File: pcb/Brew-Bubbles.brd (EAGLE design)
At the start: 25.5 x 28.7 mm, 10 parts, among them U1 GP1A57HR, U2 WEMOS-D1-MINI

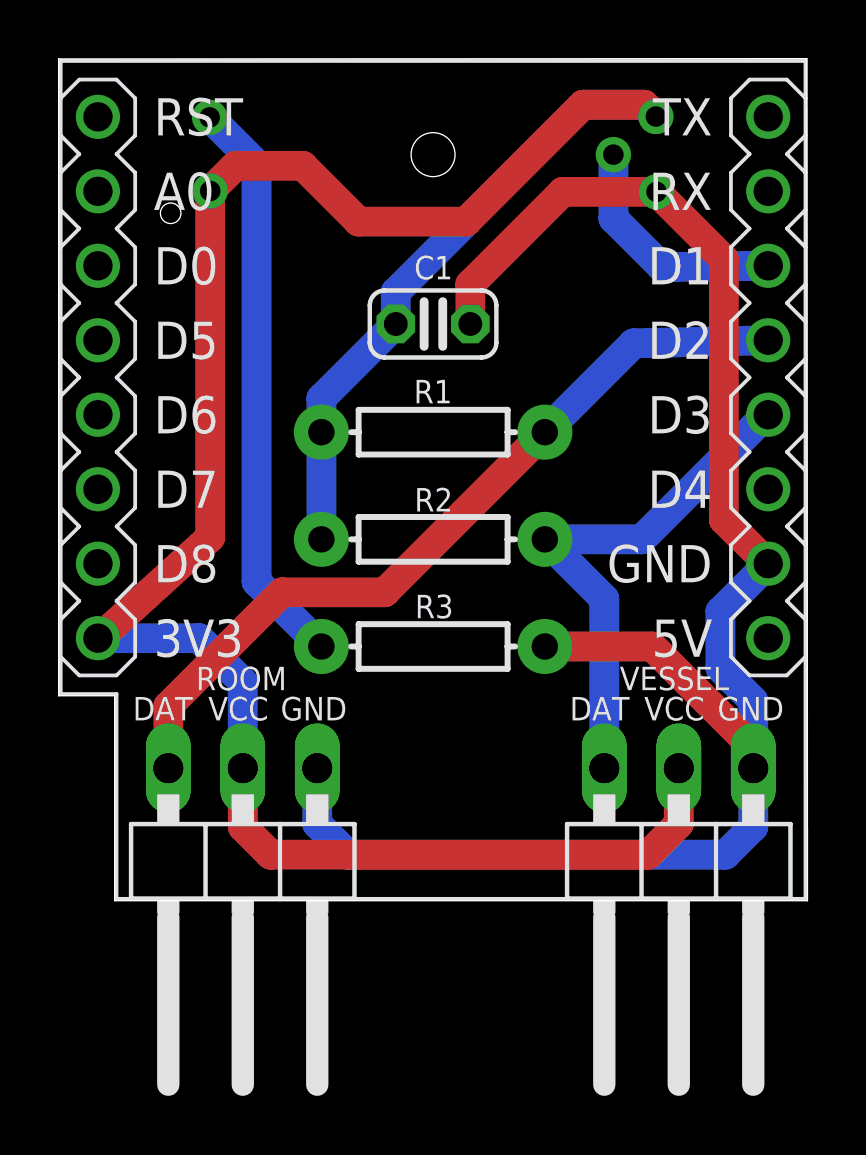
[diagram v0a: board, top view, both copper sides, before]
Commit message: Add decoupling caps to 3v3 and 5v
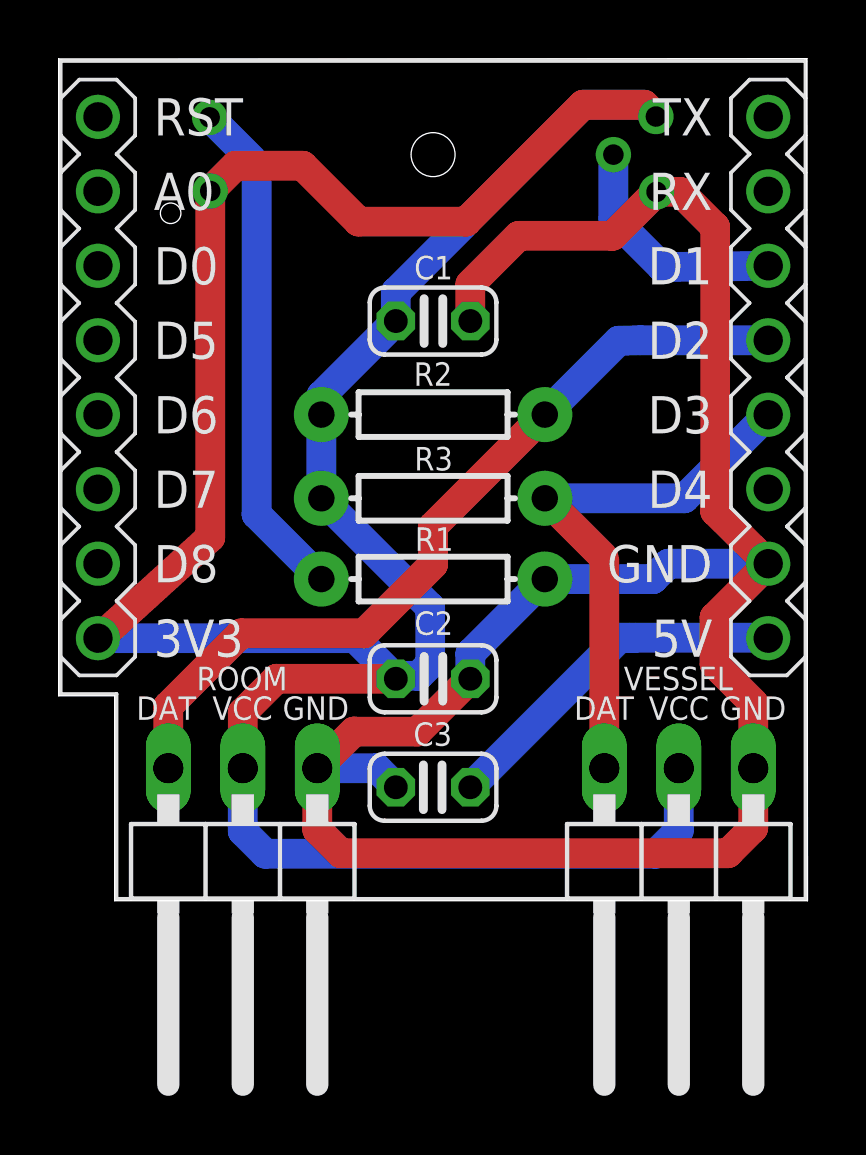
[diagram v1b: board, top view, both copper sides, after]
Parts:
- added C2, C3: 0.1μF, rcl:C025-024X044
- R1: value 2.2kΩ -> 150Ω
- R3: value 150Ω -> 2.2kΩ
- moved R3 5.05 mm to (12.8, 13.8)
- moved R1 5.01 mm to (12.8, 11.0)
- moved R2 4.25 mm to (12.8, 16.6)
- moved C1 0.10 mm to (12.8, 19.8)
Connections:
- net 3V3: now also C2.1, R3.P$2; no longer R1.P$2
- net 5V: now also C3.1
- net D2: now also R2.P$1; no longer R1.P$1
- net D3: now also R3.P$1; no longer R2.P$1
- net GND: now also C2.2, C3.2, R1.P$1; no longer R3.P$1
- net PD1: now also R1.P$2; no longer R3.P$2
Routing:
- net 3V3: track 84.5 -> 101.7 mm
- net GND: track 60.2 -> 73.3 mm
- net 5V: track 0.00 -> 12.3 mm
- net PD1: track 19.6 -> 17.3 mm
- net D3: track 18.0 -> 18.8 mm
- net D2: track 27.7 -> 28.5 mm
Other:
- board text added: "Brew Bubbles v1.0 by @LBussy brewbubbles.com"
- board text removed: "Brew Bubbles v1.0 by @LBussy www.brewbubbles.com"

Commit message: Reversed R1 and R3
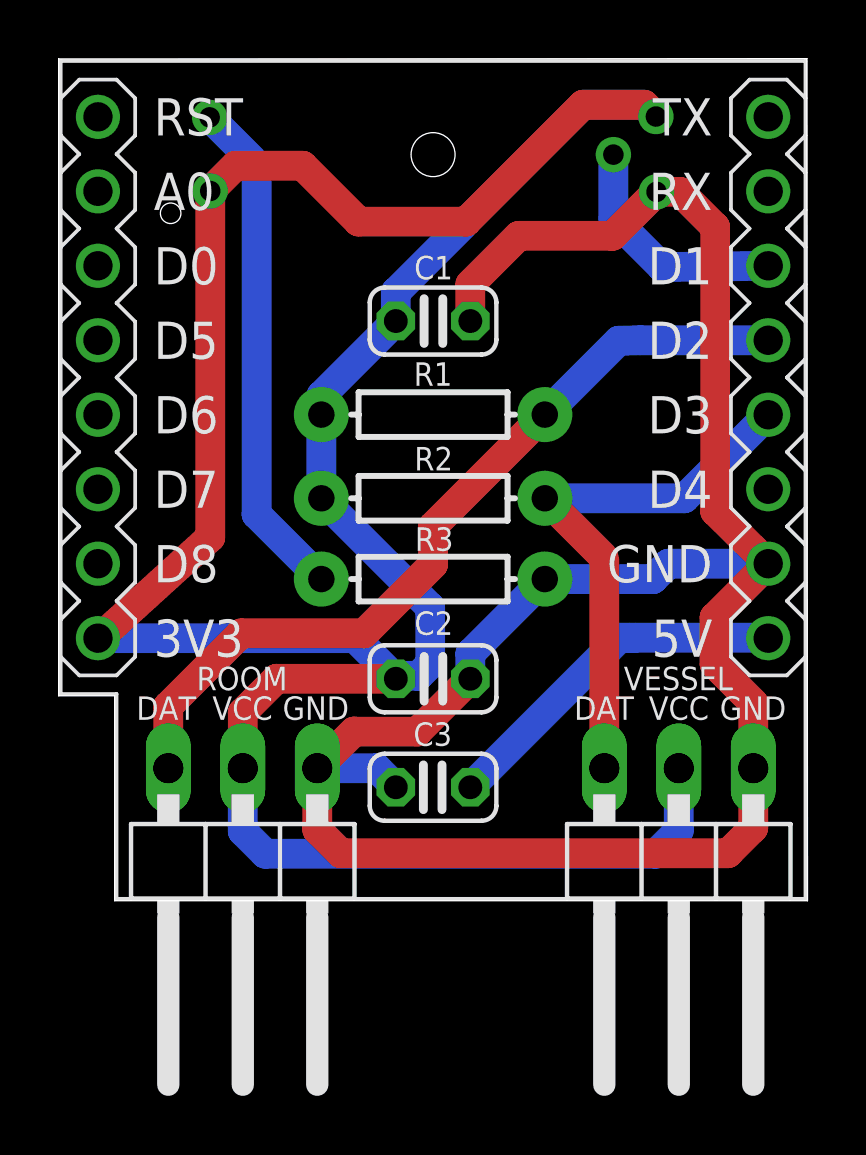
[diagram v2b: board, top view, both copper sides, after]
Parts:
- R1: value 150Ω -> 2.2kΩ
- R3: value 2.2kΩ -> 150Ω
- moved R1 5.61 mm to (12.8, 16.6)
- moved R2 2.85 mm to (12.8, 13.8)
- moved R3 2.75 mm to (12.8, 11.0)
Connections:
- net 3V3: now also R1.P$2; no longer R3.P$2
- net D2: now also R1.P$1; no longer R2.P$1
- net D3: now also R2.P$1; no longer R3.P$1
- net GND: now also R3.P$1; no longer R1.P$1
- net PD1: now also R3.P$2; no longer R1.P$2
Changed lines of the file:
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@@
 <?xml version="1.0" encoding="utf-8"?>
 <!DOCTYPE eagle SYSTEM "eagle.dtd">
-<eagle version="9.5.0">
+<eagle version="9.4.2">
 <drawing>
 <settings>
@@
 <elements>
 <element name="U2" library="diy-modules" package="WEMOS-D1-MINI-SHIELD" value="WEMOS-D1-MINI" x="12.8" y="14.7" smashed="yes"/>
-<element name="R2" library="SparkFun-Resistors" package="AXIAL-0.3" value="2.2kΩ" x="12.8" y="16.61" smashed="yes" rot="R180">
+<element name="R1" library="SparkFun-Resistors" package="AXIAL-0.3" value="2.2kΩ" x="12.8" y="16.61" smashed="yes" rot="R180">
 <attribute name="NAME" x="12.14" y="18.394" size="0.8" layer="25" font="vector" ratio="14" rot="R180" align="bottom-right"/>
 <attribute name="PROD_ID" value="RES-8371" x="12.8" y="16.61" size="1.778" layer="27" rot="R180" display="off"/>
@@
 <attribute name="POPULARITY" value="17" x="21.18" y="0.74" size="1.778" layer="27" rot="R180" display="off"/>
 </element>
-<element name="R3" library="SparkFun-Resistors" package="AXIAL-0.3" value="2.2kΩ" x="12.8" y="13.7554" smashed="yes" rot="R180">
+<element name="R2" library="SparkFun-Resistors" package="AXIAL-0.3" value="2.2kΩ" x="12.8" y="13.7554" smashed="yes" rot="R180">
 <attribute name="NAME" x="12.1612" y="15.506" size="0.8" layer="25" font="vector" ratio="14" rot="R180" align="bottom-right"/>
 <attribute name="PROD_ID" value="RES-8371" x="12.8" y="13.7554" size="1.778" layer="27" rot="R180" display="off"/>
@@
 <attribute name="SF_ID" value="SEN-09299" x="12.8" y="25.4762" size="1.778" layer="28" rot="MR180" display="off"/>
 </element>
-<element name="R1" library="SparkFun-Resistors" package="AXIAL-0.3" value="150Ω" x="12.8" y="11.0008" smashed="yes" rot="R180">
+<element name="R3" library="SparkFun-Resistors" package="AXIAL-0.3" value="150Ω" x="12.8" y="11.0008" smashed="yes" rot="R180">
 <attribute name="NAME" x="12.18" y="12.7648" size="0.8" layer="25" font="vector" ratio="14" rot="R180" align="bottom-right"/>
 <attribute name="PROD_ID" value="RES-8371" x="12.8" y="11.0008" size="1.778" layer="27" rot="R180" display="off"/>
@@
 <signal name="GND">
 <contactref element="U2" pad="JP2.7"/>
-<contactref element="R1" pad="P$1"/>
+<contactref element="R3" pad="P$1"/>
 <contactref element="U1" pad="5"/>
 <wire x1="24.23" y1="11.525" x2="24.23" y2="11.525696875" width="1.016" layer="1"/>
@@
 <contactref element="U1" pad="1"/>
 <contactref element="U1" pad="3"/>
-<contactref element="R3" pad="P$2"/>
 <contactref element="R2" pad="P$2"/>
+<contactref element="R1" pad="P$2"/>
 <wire x1="5.2" y1="24.2362" x2="5.2" y2="12.42035" width="1.016" layer="1"/>
 <wire x1="5.2" y1="12.42035" x2="1.37383125" y2="8.9408" width="1.016" layer="1"/>
@@
 <signal name="D2">
 <contactref element="U2" pad="JP2.4"/>
-<contactref element="R2" pad="P$1"/>
+<contactref element="R1" pad="P$1"/>
 <wire x1="16.61" y1="16.61" x2="19.1280875" y2="19.1280875" width="1.016" layer="16"/>
 <wire x1="19.866071875" y1="19.145" x2="19.1280875" y2="19.1280875" width="1.016" layer="16"/>
@@
 <contactref element="U2" pad="JP2.5"/>
 <wire x1="24.2209" y1="16.605" x2="24.23" y2="16.605" width="1.016" layer="16"/>
-<contactref element="R3" pad="P$1"/>
+<contactref element="R2" pad="P$1"/>
 <contactref element="VESSEL" pad="3"/>
 <wire x1="16.61" y1="13.7554" x2="21.3713" y2="13.7554" width="1.016" layer="16"/>
@@
 <signal name="PD1">
 <contactref element="U1" pad="2"/>
-<contactref element="R1" pad="P$2"/>
+<contactref element="R3" pad="P$2"/>
 <wire x1="8.99" y1="11.0008" x2="6.78" y2="13.2108" width="1.016" layer="16"/>
 <wire x1="6.78" y1="25.1462" x2="5.18" y2="26.7462" width="1.016" layer="16"/>
